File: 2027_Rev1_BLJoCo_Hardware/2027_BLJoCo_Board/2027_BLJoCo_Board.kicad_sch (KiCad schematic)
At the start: 30 parts, among them J2 Conn_01x02, J4 Conn_01x02, J5 Conn_01x06, J6 Conn_01x02, J7 Conn_01x04, J8 Conn_01x02, Q1 Q_PMOS, U1 STM32F072C8T6, U3 SN65HVD232, U4 AP63203WU

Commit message: BLJoCo
Final updates before schematic review
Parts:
- removed C1: 100nF, symbol Device:C
- removed C2: 470nF, symbol Device:C
- removed D?: >=3v3, Package_SON:WSON-6-1EP_2x2mm_P0.65mm_EP1x1.6mm, symbol Device:D_TVS
- removed Q1: Q_PMOS, symbol Device:Q_PMOS
- removed R1: 1k, symbol Device:R_US
- added C?: 100uf, Capacitor_SMD:C_0603_1608Metric_Pad1.08x0.95mm_HandSolder, symbol Device:C_Polarized
- added D3: MMSZ5240BT1G, MRDT_Devices:SOD-123_ONS-L, symbol MRDT_Devices:MMSZ5240BT1G
- added H1: MountingHole, Module:Maple_Mini, symbol Mechanical:MountingHole
- added H2: MountingHole, symbol Mechanical:MountingHole
- added MOSFET1: TPC8132_LQS, MRDT_Devices:SOP-8_TOS-L, symbol MRDT_Devices:TPC8132_LQS
- added R3: 1k, Resistor_SMD:R_0603_1608Metric_Pad0.98x0.95mm_HandSolder, symbol Device:R_US
- D1: value 15V -> D_Zener; footprint (none) -> Diode_THT:D_DO-41_SOD81_P10.16mm_Horizontal
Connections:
- net +24V: now also D3.1, MOSFET1.1 (S), MOSFET1.2, MOSFET1.3; no longer D1.1 (K)
- net +3.3V: now also D1.1 (K)
- net GND: now also D1.2 (A), C?.2, R3.2
- net Vaux: now also C?.1, MOSFET1.5 (D), MOSFET1.6, MOSFET1.7, MOSFET1.8
- new net: D3.2, MOSFET1.4 (G), R3.1
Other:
- note added: "Mounting Holes"

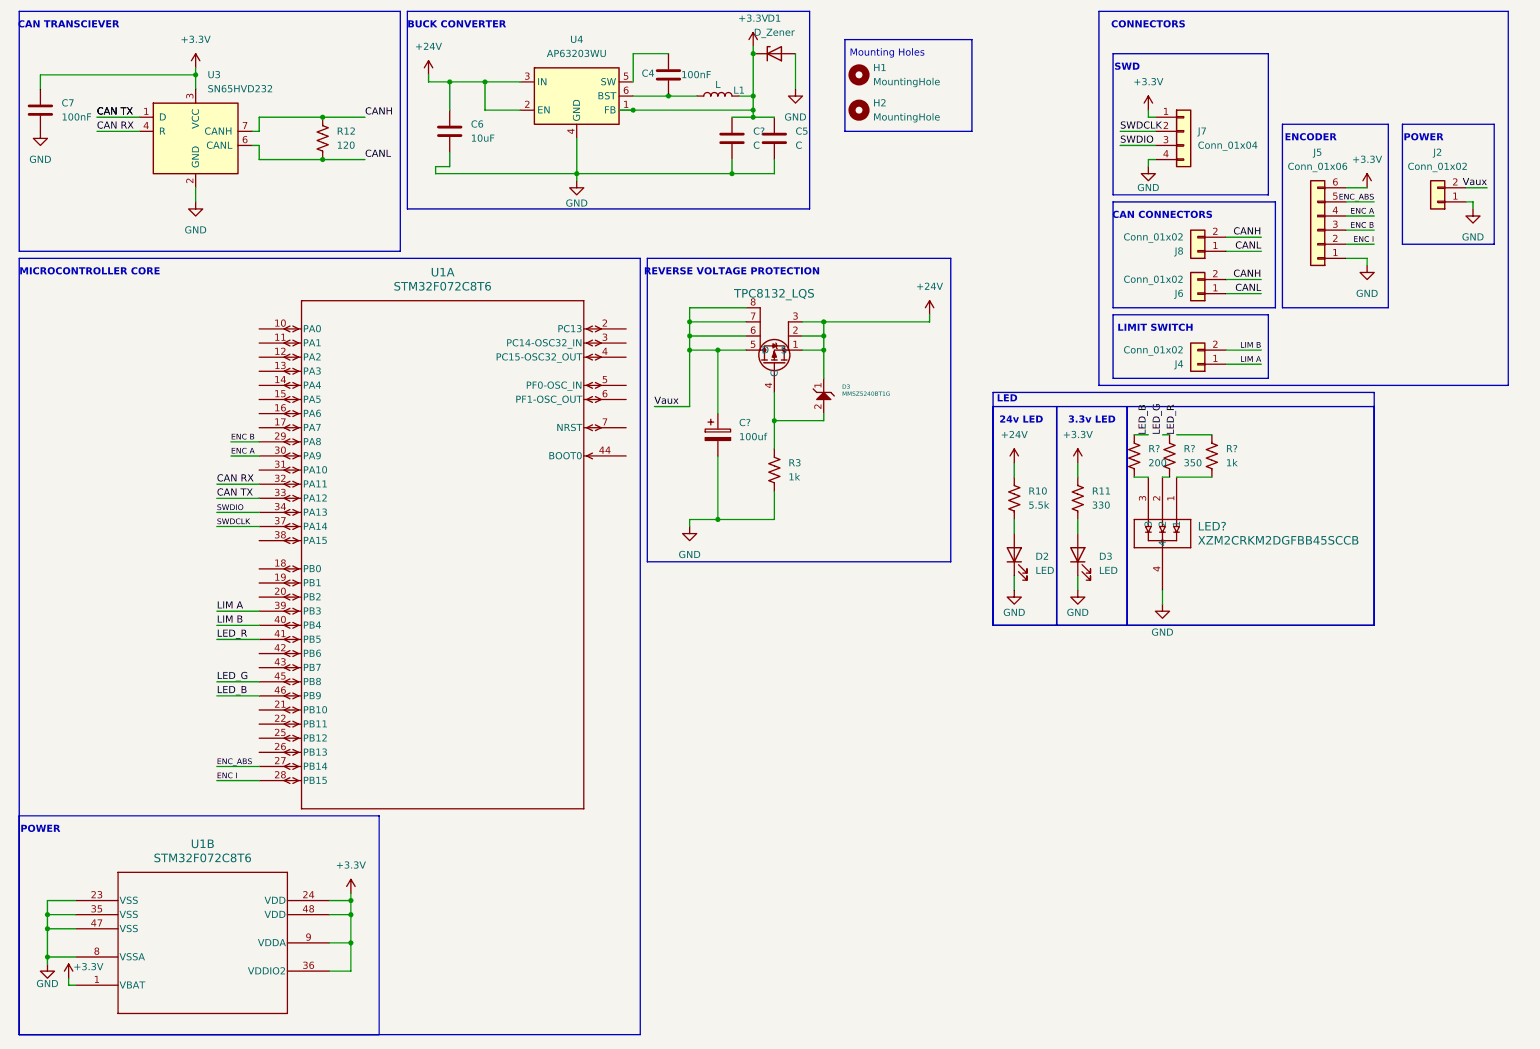
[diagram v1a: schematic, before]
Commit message: STM32 footprint and some components fixed
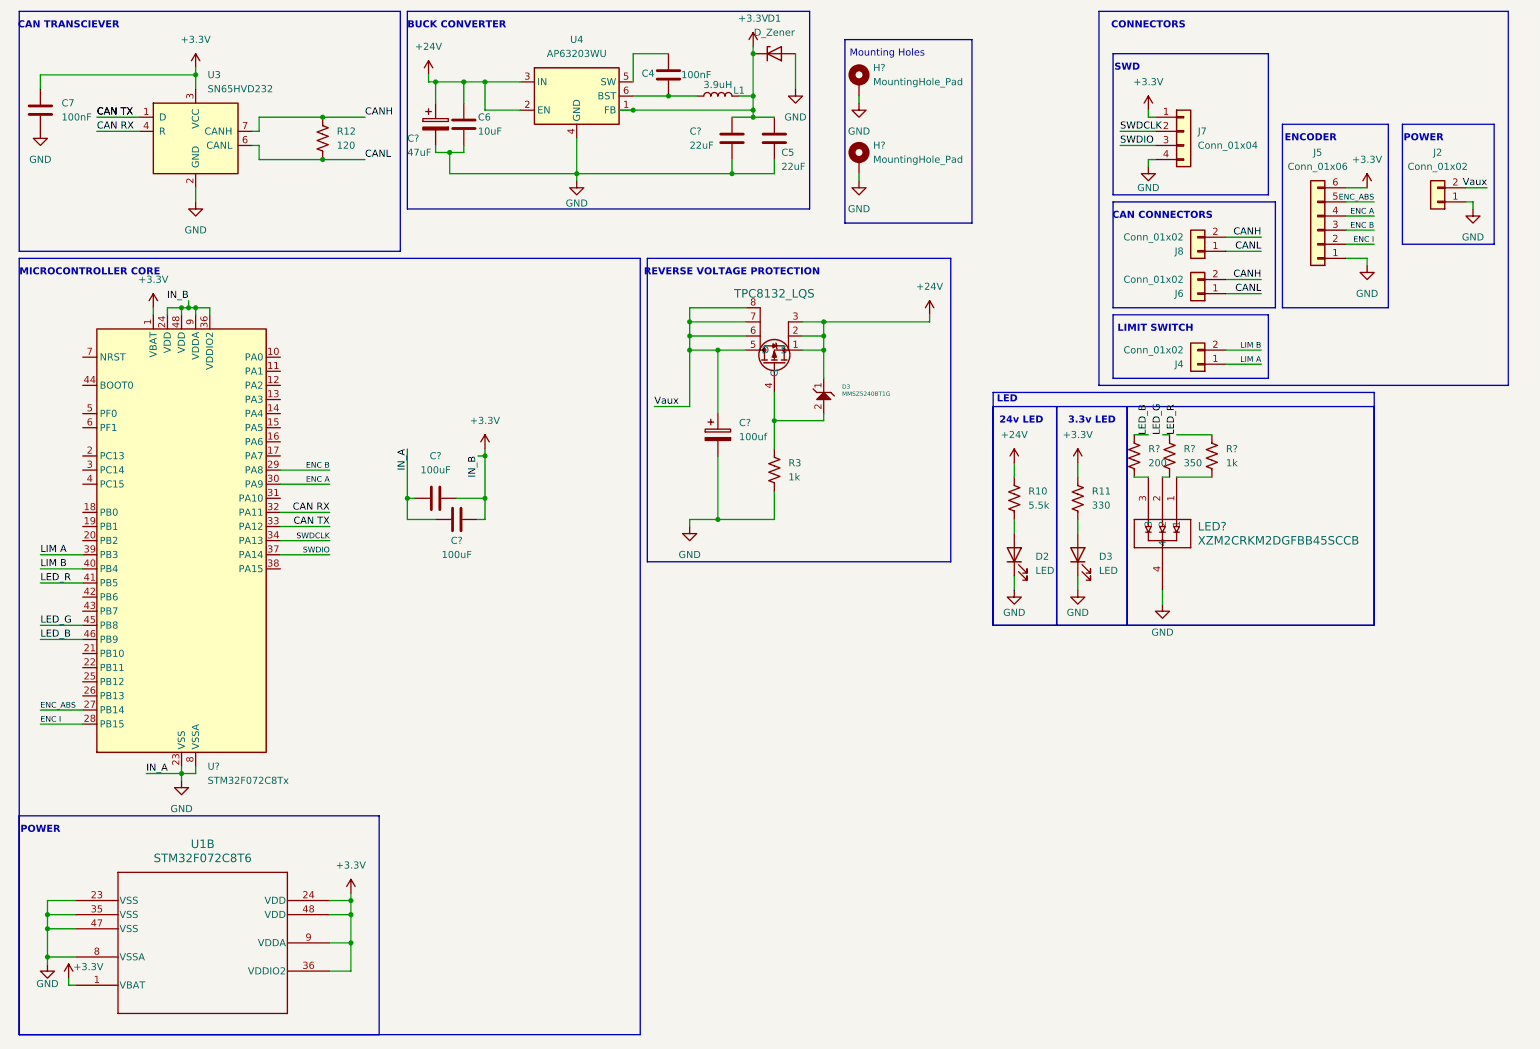
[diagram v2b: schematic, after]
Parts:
- removed H1: MountingHole, Module:Maple_Mini, symbol Mechanical:MountingHole
- removed H2: MountingHole, symbol Mechanical:MountingHole
- removed unit 1 of U1
- added C? (x2): 100uF, symbol Device:C
- added C?: 47uF, symbol Device:C_Polarized
- added H? (x2): MountingHole_Pad, symbol Mechanical:MountingHole_Pad
- added U?: STM32F072C8Tx, Package_QFP:LQFP-48_7x7mm_P0.5mm, symbol MCU_ST_STM32F0:STM32F072C8Tx
- C5, C?: value C -> 22uF
- L1: value L -> 3.9uH
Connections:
- net +24V: now also C?.1
- net +3.3V: now also C?.1, C?.1, U?.1 (VBAT), U?.24 (VDD), U?.36 (VDDIO2), U?.48 (VDD), U?.9 (VDDA)
- net CAN RX: now also U?.32 (PA11)
- net CAN TX: now also U?.33 (PA12)
- net ENC A: now also U?.30 (PA9)
- net ENC B: now also U?.29 (PA8)
- net ENC I: now also U?.28 (PB15)
- net ENC_ABS: now also U?.27 (PB14)
- net GND: now also C?.2, C?.2, C?.2, H?.1, H?.1, U?.23 (VSS), U?.35 (VSS), U?.47 (VSS), U?.8 (VSSA)
- net LED_B: now also U?.46 (PB9)
- net LED_G: now also U?.45 (PB8)
- net LED_R: now also U?.41 (PB5)
- net LIM A: now also U?.39 (PB3)
- net LIM B: now also U?.40 (PB4)
- net SWDCLK: now also U?.34 (PA13)
- net SWDIO: now also U?.37 (PA14)
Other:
- moved on the sheet: C6

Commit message: Button's Capacitors and connector updated.
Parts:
- removed J4: Conn_01x02, symbol Connector_Generic:Conn_01x02
- removed R?: 350, symbol Device:R_US
- removed R?: 200, symbol Device:R_US
- removed R?: 1k, symbol Device:R_US
- added C2, C?: 100nF, symbol Device:C
- added C?: 220uf, Capacitor_SMD:C_0603_1608Metric_Pad1.08x0.95mm_HandSolder, symbol Device:C_Polarized
- added D5, D?: D_TVS, Diode_SMD:D_0603_1608Metric_Pad1.05x0.95mm_HandSolder, symbol Device:D_TVS
- added J?: Conn_01x03, Package_TO_SOT_SMD:SOT-23-5, symbol Connector_Generic:Conn_01x03
- added JP1, JP?: Jumper_2_Open, Package_LCC:PLCC-84_29.3x29.3mm_P1.27mm, symbol Jumper:Jumper_2_Open
- added TP?: TestPoint, Package_TO_SOT_SMD:SOT-23-5, symbol Connector:TestPoint
- C?: value 100uf -> 220uf
- D2, D3: value LED -> GREEN
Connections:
- net +3.3V: now also TP?.1
- net GND: now also C2.2, C?.2, C?.2, D5.1 (A1), D?.1 (A1), J?.3 (Pin_3), JP1.1 (A), JP?.1 (A)
- net LIM A: now also J?.1 (Pin_1)
- net LIM B: now also J?.2 (Pin_2)
- net LED_G_Out: now reaches LED?.2
- net boot: now reaches U?.44 (BOOT0)
- net boot: now also C?.1, D?.2 (A2), JP?.2 (B)
- net nrst: now reaches U?.7 (NRST)
- net nrst: now also C2.1, D5.2 (A2), JP1.2 (B)
- net LED_R_Out: now reaches LED?.1
- net LED_B_Out: now reaches LED?.3
- net Vaux renamed V_AUX
- net V_AUX: now also C?.1
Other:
- note added: "Boot Button"
- note added: "Buttons"
- note added: "Reset Button"
- moved on the sheet: C?, D2, D3, H?, LED?, R10, R11

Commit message: MOSFET's added for RGB LED circuit
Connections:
- net LED_B_Out renamed Led_B_Out
- net LED_G_Out renamed Led_G_Out
- net LED_R_Out renamed Led_R_Out
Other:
- added sheet LED Mosfets (untitled.kicad_sch)

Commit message: Updated Power Circuit
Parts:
- removed C? (x2): 100uF, symbol Device:C
- removed U1: STM32F072C8T6, LQFP48-7x7mm, symbol STM32F072C8T6:STM32F072C8T6
- added C20, C24: 4.7uF, symbol Device:C
- added C21, C25, C26, C27: 100nF, symbol Device:C
- added C22: 10nF, symbol Device:C
- added C23: 1uF, symbol Device:C
- gave numbers to parts that had none: 13
- renumbered D3 to D6
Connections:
- net +3.3V: now also C20.1, C21.1, C22.1, C23.1, C24.1, C25.1, C26.1, C27.1; no longer U1.36 (VDDIO2)
- net GND: now also C20.2, C21.2, C22.2, C23.2, C24.2, C25.2, C26.2, C27.2
- new net VDDI02: U1.36 (VDDIO2)
- no-connect marks 0 -> 24
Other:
- moved on the sheet: U1

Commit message: Footprints assigned
Footprints assigned and board almost complete.
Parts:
- removed C1: 47uF, symbol Device:C_Polarized
- removed C3: 220uf, Capacitor_SMD:C_0603_1608Metric_Pad1.08x0.95mm_HandSolder, symbol Device:C_Polarized
- C10, C2, C20, C21, C22, C23, C24, C25, C26, C27, C4, C5, C6, C7, C8: footprint (none) -> Capacitor_SMD:C_0603_1608Metric_Pad1.08x0.95mm_HandSolder
- C9: value 220uf -> 100uf; footprint Capacitor_SMD:C_0603_1608Metric_Pad1.08x0.95mm_HandSolder -> Capacitor_THT:CP_Radial_D8.0mm_P3.50mm
- D1: value D_Zener -> MMSZ4685-TP; footprint Diode_THT:D_DO-41_SOD81_P10.16mm_Horizontal -> Diode_SMD:D_SOD-523
- D2, D3: footprint (none) -> LED_SMD:LED_0603_1608Metric_Pad1.05x0.95mm_HandSolder
- D6: footprint MRDT_Devices:SOD-123_ONS-L -> Diode_SMD:D_SOD-123
- H1, H2: footprint (none) -> MountingHole:MountingHole_3.2mm_M3_Pad
- J1: footprint Package_TO_SOT_SMD:SOT-23-5 -> Connector_Wire:SolderWire-0.5sqmm_1x03_P4.6mm_D0.9mm_OD2.1mm
- J2: footprint (none) -> Connector_Wire:SolderWire-1.5sqmm_1x02_P6mm_D1.7mm_OD3mm
- J5: footprint (none) -> Connector_Wire:SolderWire-0.5sqmm_1x06_P4.6mm_D0.9mm_OD2.1mm
- J6, J8: footprint (none) -> Connector_Wire:SolderWire-0.5sqmm_1x02_P4.6mm_D0.9mm_OD2.1mm
- J7: footprint (none) -> Connector_PinHeader_2.54mm:PinHeader_1x04_P2.54mm_Vertical
- JP1, JP2: footprint Package_LCC:PLCC-84_29.3x29.3mm_P1.27mm -> Jumper:SolderJumper-2_P1.3mm_Open_Pad1.0x1.5mm
- L1: footprint (none) -> Inductor:IND_TFM252012ALMA1R0MTAA_TDK
- LED1: footprint PLCC4_3p5x2p8_SLD -> RGBLED:PLCC4_3p5x2p8_SLD
- MOSFET1: footprint MRDT_Devices:SOP-8_TOS-L -> Package_SO:SOIC-8_3.9x4.9mm_P1.27mm
- R10, R11, R12: footprint (none) -> Resistor_SMD:R_0603_1608Metric_Pad0.98x0.95mm_HandSolder
- TP1: footprint Package_TO_SOT_SMD:SOT-23-5 -> TestPoint:TestPoint_Pad_D1.5mm
